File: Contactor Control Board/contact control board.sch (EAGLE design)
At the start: 34 parts, among them Q1 2n2222, Q3 2n2222, Q4 MOSFET-NCHANNELFQP30N06L, Q5 MOSFET-NCHANNELFQP30N06L, U1 MM74HC125N

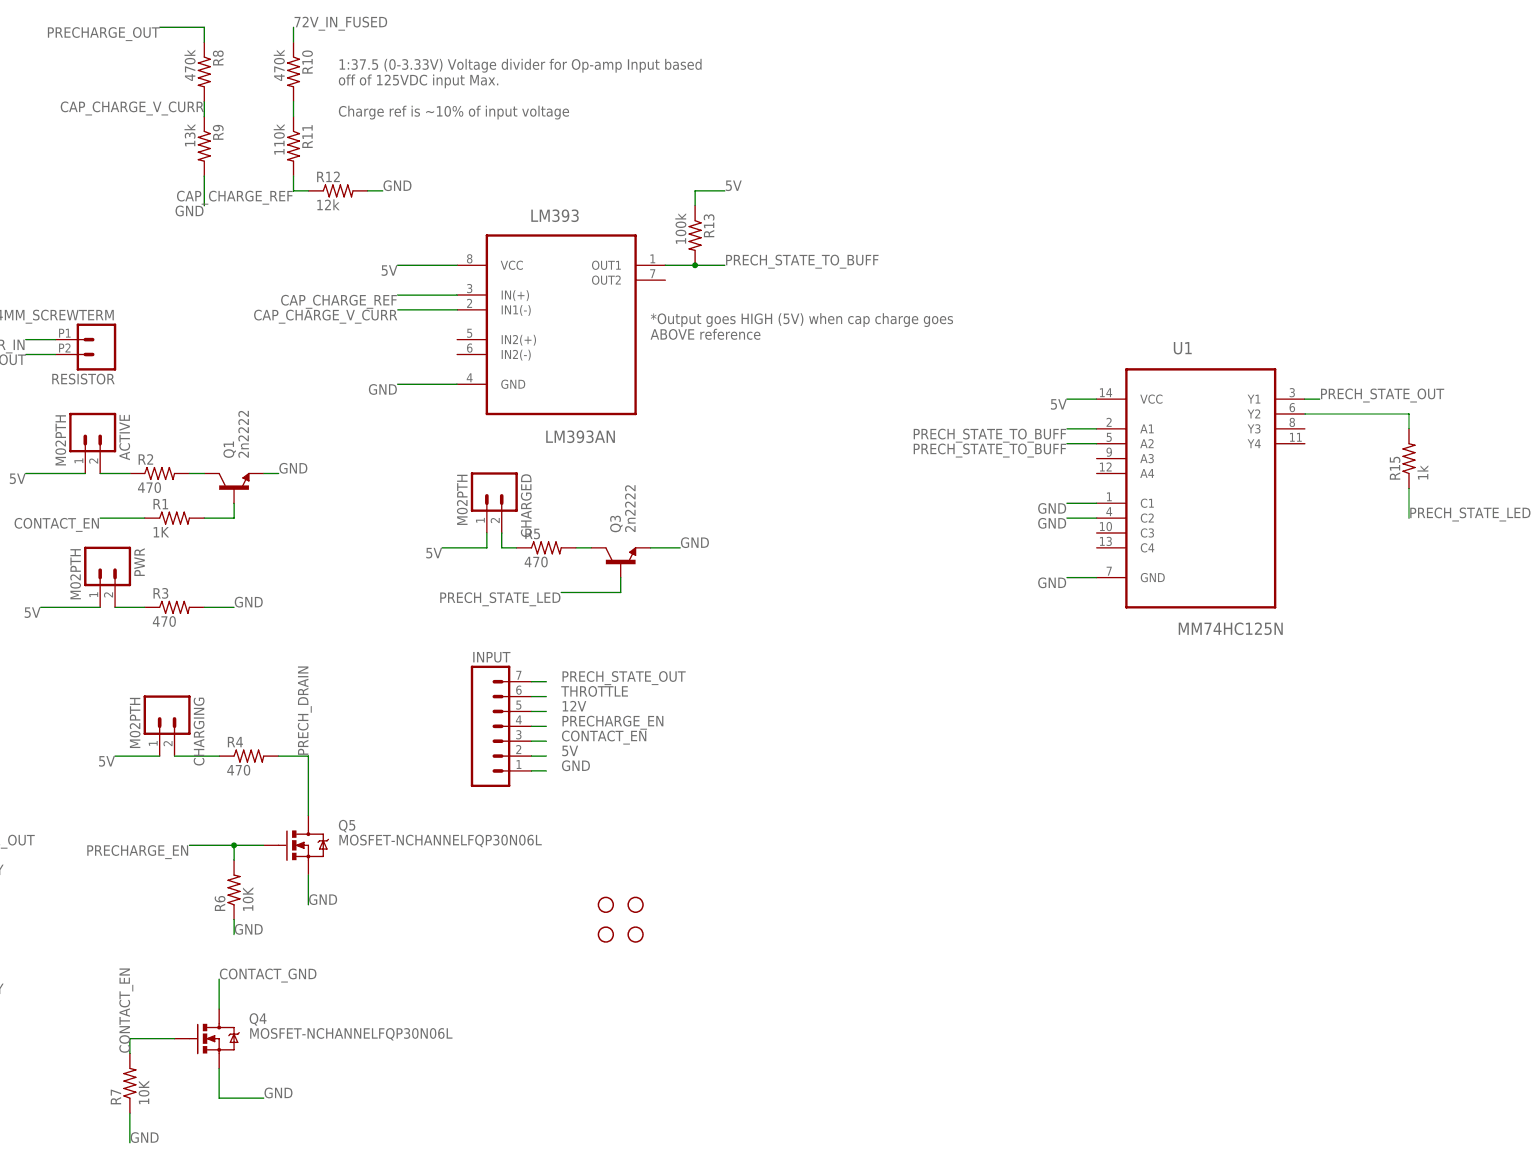
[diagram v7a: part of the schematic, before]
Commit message: Mostly routed. Replaced all thru-hole with SMD components. Much smaller!
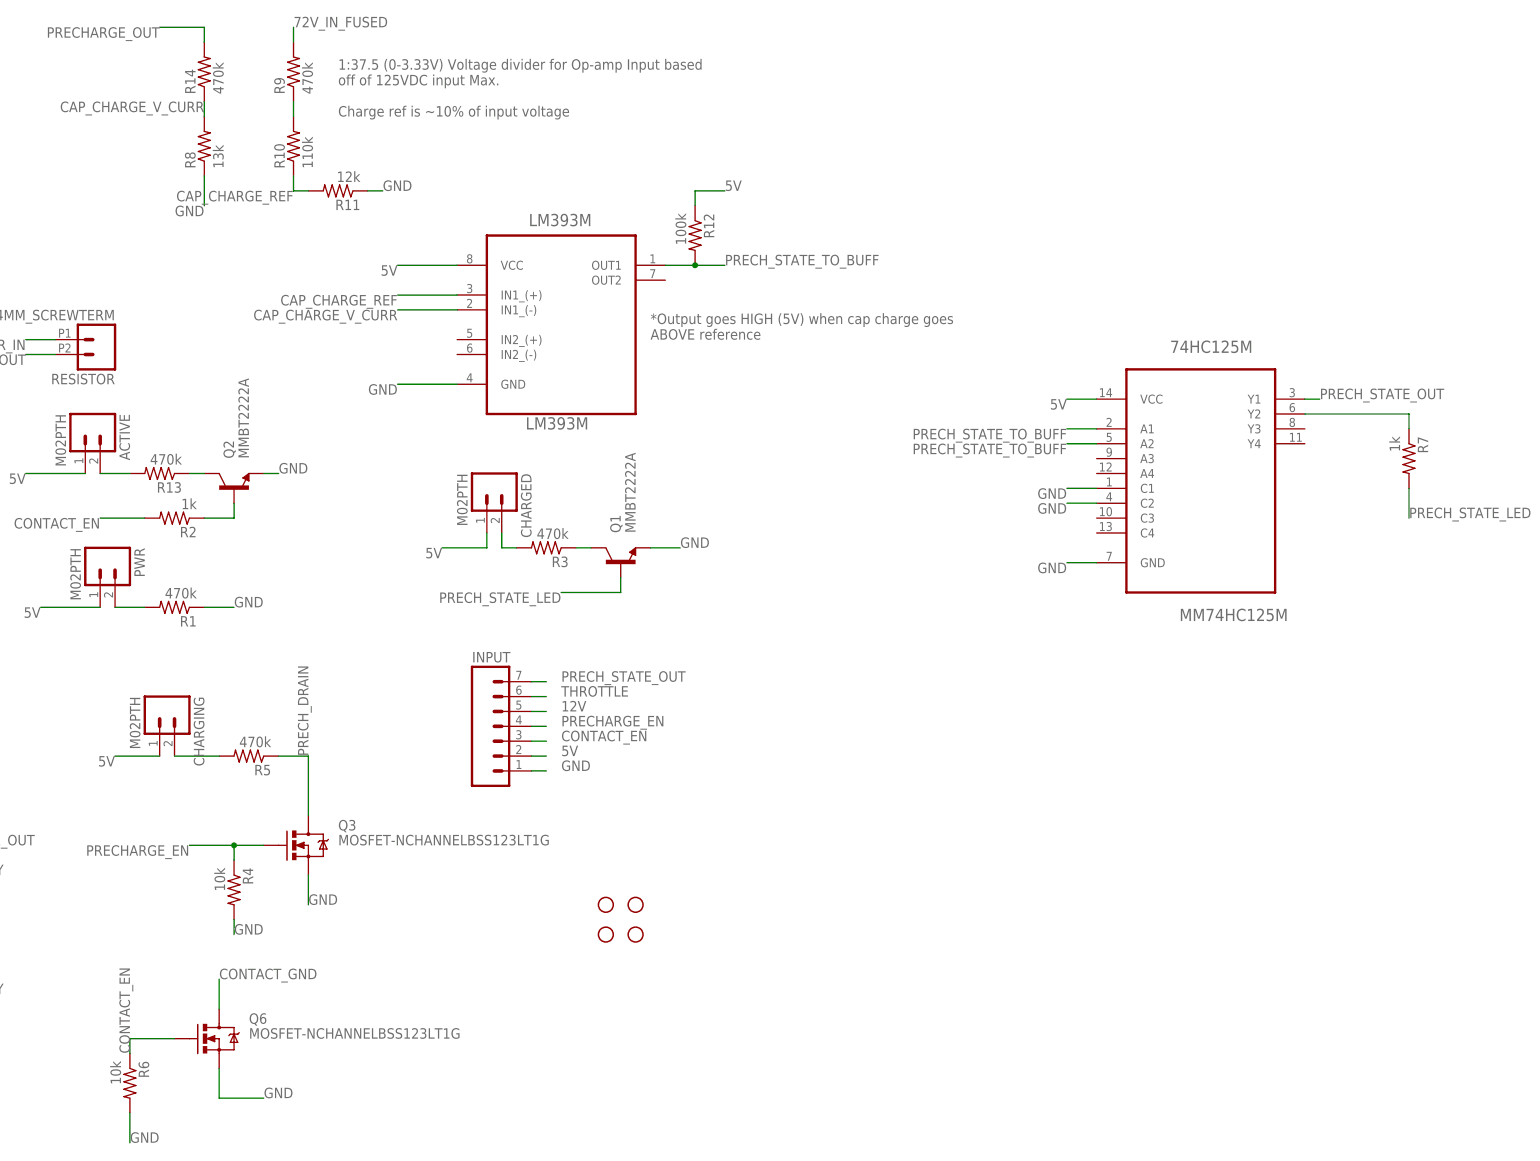
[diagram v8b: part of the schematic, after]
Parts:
- removed LM393: LM393AN, Fairchild_By_element14_Batch_1:LM393AN
- removed Q4, Q5: MOSFET-NCHANNELFQP30N06L, SparkFun-DiscreteSemi:MOSFET-NCHANNELFQP30N06L
- removed R15: 1k, SparkFun-Resistors:RESISTORPTH-1/4W
- removed U1: MM74HC125N, mm74hc125n:MM74HC125N
- added 74HC125M: MM74HC125M, Fairchild_By_element14_Batch_1:MM74HC125M
- added LM393M: LM393M, Fairchild_By_element14_Batch_1:LM393M
- added Q2: MMBT2222A, SparkFun-DiscreteSemi:TRANSISTOR_NPNMMBT2222A
- added Q6: MOSFET-NCHANNELBSS123LT1G, SparkFun-DiscreteSemi:MOSFET-NCHANNELBSS123LT1G
- added R14: 470k, SparkFun-Resistors:RESISTOR0603-RES
- Q1: value 2n2222 -> MMBT2222A; device SparkFun-DiscreteSemi:TRANSISTOR_NPNTO-92-AMMO -> SparkFun-DiscreteSemi:TRANSISTOR_NPNMMBT2222A
- Q3: value 2n2222 -> MOSFET-NCHANNELBSS123LT1G; device SparkFun-DiscreteSemi:TRANSISTOR_NPNTO-92-AMMO -> SparkFun-DiscreteSemi:MOSFET-NCHANNELBSS123LT1G
- R1: value 1K -> 470k; device SparkFun-Resistors:RESISTORPTH-1/4W -> SparkFun-Resistors:RESISTOR0603-RES
- R10: value 470k -> 110k; device SparkFun-Resistors:RESISTORPTH-1/4W -> SparkFun-Resistors:RESISTOR0603-RES
- R11: value 110k -> 12k; device SparkFun-Resistors:RESISTORPTH-1/4W -> SparkFun-Resistors:RESISTOR0603-RES
- R12: value 12k -> 100k; device SparkFun-Resistors:RESISTORPTH-1/4W -> SparkFun-Resistors:RESISTOR0603-RES
- R13: value 100k -> 470k; device SparkFun-Resistors:RESISTORPTH-1/4W -> SparkFun-Resistors:RESISTOR0603-RES
- R2: value 470 -> 1k; device SparkFun-Resistors:RESISTORPTH-1/4W -> SparkFun-Resistors:RESISTOR0603-RES
- R3, R5: value 470 -> 470k; device SparkFun-Resistors:RESISTORPTH-1/4W -> SparkFun-Resistors:RESISTOR0603-RES
- R4: value 470 -> 10k; device SparkFun-Resistors:RESISTORPTH-1/4W -> SparkFun-Resistors:RESISTOR0603-RES
- R6: value 10K -> 10k; device SparkFun-Resistors:RESISTORPTH-1/4W -> SparkFun-Resistors:RESISTOR0603-RES
- R7: value 10K -> 1k; device SparkFun-Resistors:RESISTORPTH-1/4W -> SparkFun-Resistors:RESISTOR0603-RES
- R8: value 470k -> 13k; device SparkFun-Resistors:RESISTORPTH-1/4W -> SparkFun-Resistors:RESISTOR0603-RES
- R9: value 13k -> 470k; device SparkFun-Resistors:RESISTORPTH-1/4W -> SparkFun-Resistors:RESISTOR0603-RES
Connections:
- net 5V: now also 74HC125M.VCC, LM393M.VCC, R12.1; no longer LM393.VCC, R13.1, U1.VCC
- net 72V_IN_FUSED: now also R9.2; no longer R10.1
- net CAP_CHARGE_REF: now also LM393M.IN1_(+), R10.1; no longer LM393.IN(+), R12.1
- net CAP_CHARGE_V_CURR: now also LM393M.IN1_(-), R14.1; no longer LM393.IN1(-), R9.1
- net CONTACT_EN: now also Q6.G, R2.2, R6.1; no longer Q4.G, R1.1, R7.2
- net CONTACT_GND: now also Q6.D; no longer Q4.D
- net GND: now also 74HC125M.C1, 74HC125M.C2, 74HC125M.GND, LM393M.GND, Q2.E, Q3.S, Q6.S, R1.1, R11.1, R4.2, R6.2, R8.1; no longer LM393.GND, Q3.E, Q4.S, Q5.S, R12.2, R3.2, R6.1, R7.1, R9.2, U1.C1, U1.C2, U1.GND
- net N$1: now also Q2.C, R13.1; no longer Q1.C, R2.2
- net N$12: now also R1.2; no longer R3.1
- net N$2: now also Q2.B, R2.1; no longer Q1.B, R1.2
- net N$3: now also R9.1; no longer R11.1
- net N$4: now also R3.2; no longer R5.1
- net N$5: now also Q1.C, R3.1; no longer Q3.C, R5.2
- net N$6: now also 74HC125M.Y2, R7.1; no longer R15.2, U1.Y2
- net N$7: now also R5.2; no longer R4.1
- net N$9: now also R13.2; no longer R2.1
- net PRECHARGE_EN: now also Q3.G, R4.1; no longer Q5.G, R6.2
- net PRECHARGE_OUT: now also R14.2; no longer R8.1
- net PRECH_DRAIN: now also Q3.D, R5.1; no longer Q5.D, R4.2
- net PRECH_STATE_LED: now also Q1.B, R7.2; no longer Q3.B, R15.1
- net PRECH_STATE_OUT: now also 74HC125M.Y1; no longer U1.Y1
- net PRECH_STATE_TO_BUFF: now also 74HC125M.A1, 74HC125M.A2, LM393M.OUT1, R12.2; no longer LM393.OUT1, R13.2, U1.A1, U1.A2
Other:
- moved on the sheet: Q1, R1, R10, R11, R12, R13, R2, R3, R4, R5, R6, R7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
